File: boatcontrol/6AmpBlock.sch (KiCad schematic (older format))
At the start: 15 parts, among them U7901 ULN2803A

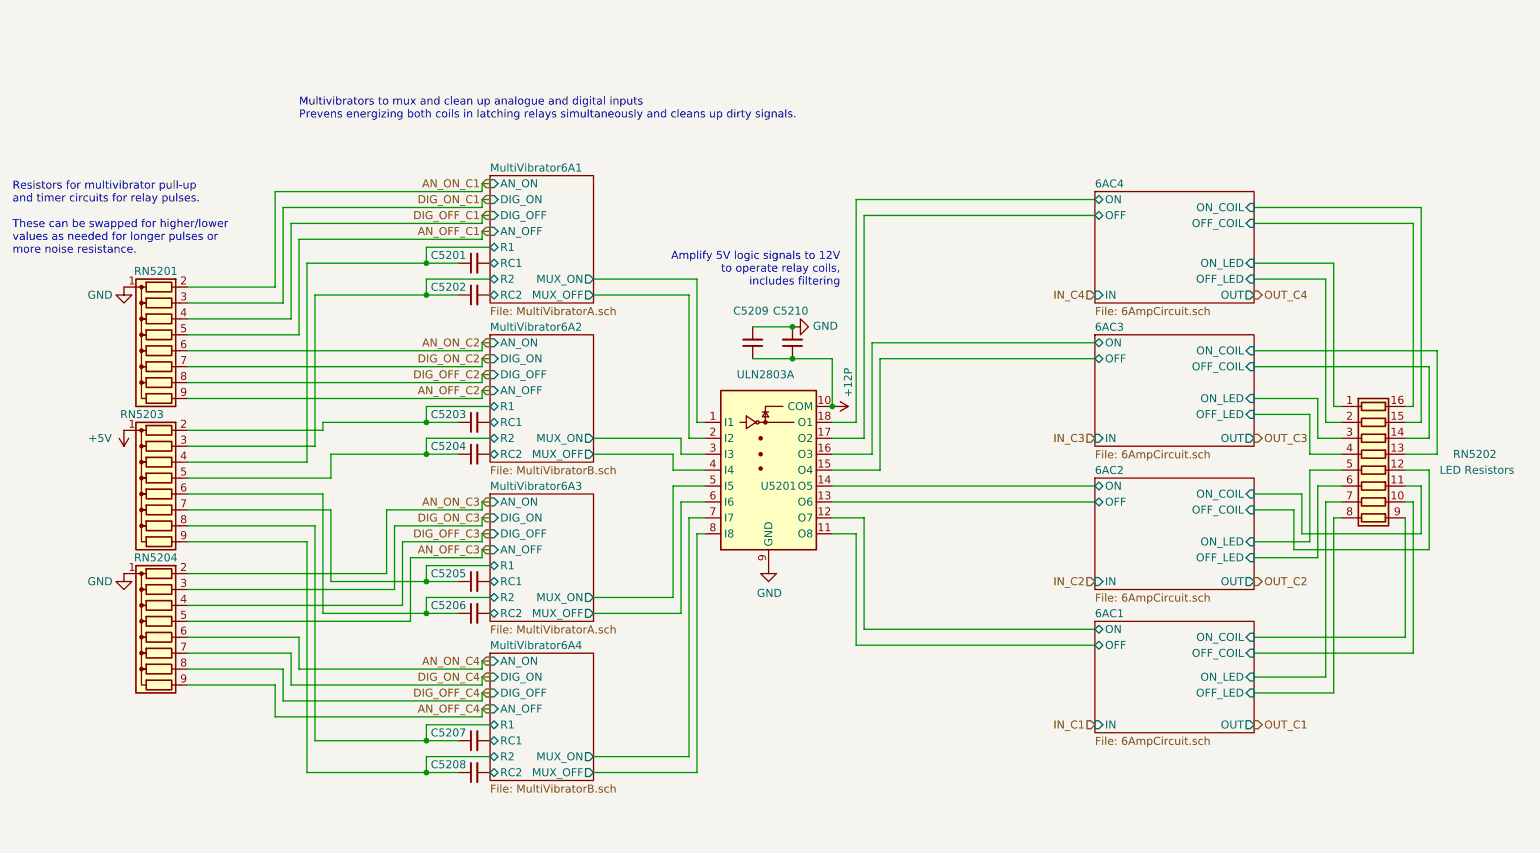
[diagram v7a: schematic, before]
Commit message: add second e-section
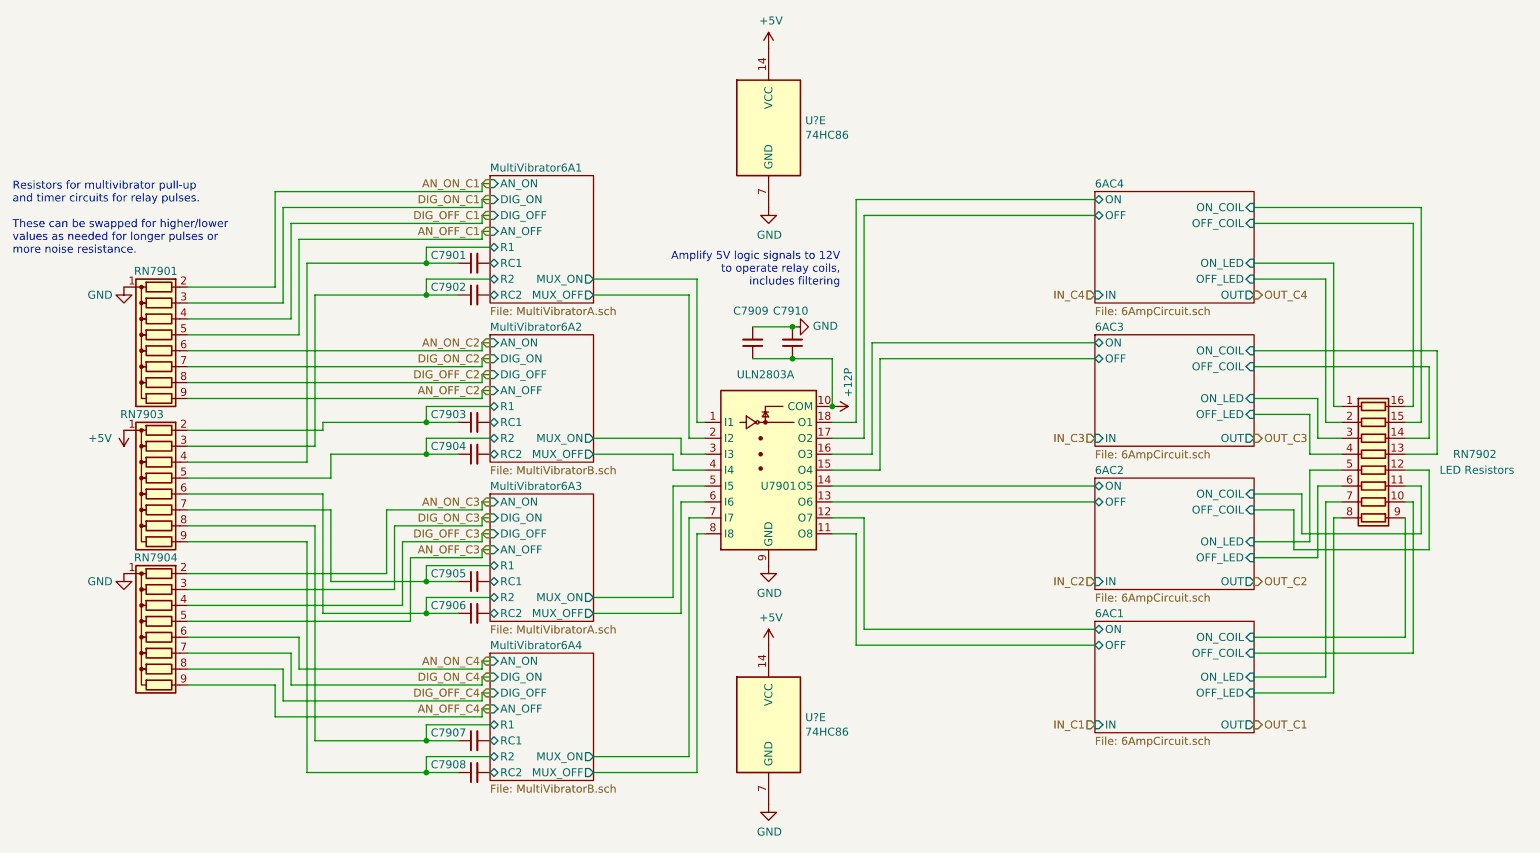
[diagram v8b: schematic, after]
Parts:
- added U? (x2): 74HC86, symbol 74xx:74HC86
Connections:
- net +5V: now also U?.14 (VCC), U?.14 (VCC)
- net GND: now also U?.7 (GND), U?.7 (GND)
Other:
- note removed: "Multivibrators to mux and clean up analogue and digital inputs\nPrevens energizing both coils in latching relays simultaneously and cleans up dirty signals."
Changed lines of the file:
@@
 $Descr A4 11693 8268
 encoding utf-8
-Sheet 40 97
+Sheet 67 97
 Title "Boat Control Hat"
 Date "2020-07-09"
@@
 AR Path="/D1BB8DB4/5F317CB5/60365AE4" Ref="#PWR07901"  Part="1"
 AR Path="/D1BB8DB4/5F746103/60365AE4" Ref="#PWR05201"  Part="1"
-F 0 "#PWR05201" H 6700 3400 50  0001 C CNN
+F 0 "#PWR07901" H 6700 3400 50  0001 C CNN
 F 1 "+12P" H 6550 3650 50  0000 C CNN
 F 2 "" H 6700 3550 50  0001 C CNN
@@
 AR Path="/D1BB8DB4/5F317CB5/60365AF1" Ref="U7901"  Part="1"
 AR Path="/D1BB8DB4/5F746103/60365AF1" Ref="U5201"  Part="1"
-F 0 "U5201" H 6250 3650 50  0000 L CNN
+F 0 "U7901" H 6250 3650 50  0000 L CNN
 F 1 "ULN2803A" H 6100 4350 50  0000 L CNN
 F 2 "Package_DIP:DIP-18_W7.62mm" H 6350 3200 50  0001 L CNN
@@
 Text HLabel 4550 4150 0    50   Output ~ 0
 AN_ON_C3
-Text Notes 3350 1750 0    50   ~ 0
-Multivibrators to mux and clean up analogue and digital inputs\nPrevens energizing both coils in latching relays simultaneously and cleans up dirty signals.
 Text Notes 6750 2800 2    50   ~ 0
 Amplify 5V logic signals to 12V\nto operate relay coils,\nincludes filtering
@@
 AR Path="/D1BB8DB4/5F317CB5/60365B03" Ref="#PWR07902"  Part="1"
 AR Path="/D1BB8DB4/5F746103/60365B03" Ref="#PWR05202"  Part="1"
-F 0 "#PWR05202" H 6300 4300 50  0001 C CNN
+F 0 "#PWR07902" H 6300 4300 50  0001 C CNN
 F 1 "GND" H 6305 4377 50  0000 C CNN
 F 2 "" H 6300 4550 50  0001 C CNN
@@
 AR Path="/D1BB8DB4/5F317CB5/60365C68" Ref="RN7902"  Part="1"
 AR Path="/D1BB8DB4/5F746103/60365C68" Ref="RN5202"  Part="1"
-F 0 "RN5202" V 10000 4450 50  0000 L CNN
+F 0 "RN7902" V 10000 4450 50  0000 L CNN
 F 1 "680Ω" V 9600 3800 50  0001 L CNN
 F 2 "BoatControl:DIP254P762X432-16P" V 10575 3950 50  0001 C CNN
@@
 AR Path="/D1BB8DB4/5F746103/62AB509B" Ref="C5201"  Part="1"
 AR Path="/D1BB8DB4/5F317CB5/62AB509B" Ref="C7901"  Part="1"
-F 0 "C5201" V 4400 2700 50  0000 L CNN
+F 0 "C7901" V 4400 2700 50  0000 L CNN
 F 1 "1µF" H 3600 2550 50  0001 L CNN
 F 2 "Capacitor_THT:C_Disc_D7.5mm_W5.0mm_P5.00mm" H 4450 2650 50  0001 C CNN
@@
 AR Path="/D1BB8DB4/5F746103/62AC1E93" Ref="C5202"  Part="1"
 AR Path="/D1BB8DB4/5F317CB5/62AC1E93" Ref="C7902"  Part="1"
-F 0 "C5202" V 4400 2900 50  0000 L CNN
+F 0 "C7902" V 4400 2900 50  0000 L CNN
 F 1 "1µF" H 3600 2750 50  0001 L CNN
 F 2 "Capacitor_THT:C_Disc_D7.5mm_W5.0mm_P5.00mm" H 4450 2850 50  0001 C CNN
@@
 AR Path="/D1BB8DB4/5F746103/62ADD9A6" Ref="C5208"  Part="1"
 AR Path="/D1BB8DB4/5F317CB5/62ADD9A6" Ref="C7908"  Part="1"
-F 0 "C5208" V 4400 5900 50  0000 L CNN
+F 0 "C7908" V 4400 5900 50  0000 L CNN
 F 1 "1µF" H 3600 5750 50  0001 L CNN
 F 2 "Capacitor_THT:C_Disc_D7.5mm_W5.0mm_P5.00mm" H 4450 5850 50  0001 C CNN
@@
 AR Path="/D1BB8DB4/5F746103/62AEACF8" Ref="C5207"  Part="1"
 AR Path="/D1BB8DB4/5F317CB5/62AEACF8" Ref="C7907"  Part="1"
-F 0 "C5207" V 4400 5700 50  0000 L CNN
+F 0 "C7907" V 4400 5700 50  0000 L CNN
 F 1 "1µF" H 3600 5550 50  0001 L CNN
 F 2 "Capacitor_THT:C_Disc_D7.5mm_W5.0mm_P5.00mm" H 4450 5650 50  0001 C CNN
@@
 AR Path="/D1BB8DB4/5F746103/62AF81A3" Ref="C5206"  Part="1"
 AR Path="/D1BB8DB4/5F317CB5/62AF81A3" Ref="C7906"  Part="1"
-F 0 "C5206" V 4400 4900 50  0000 L CNN
+F 0 "C7906" V 4400 4900 50  0000 L CNN
 F 1 "1µF" H 3600 4750 50  0001 L CNN
 F 2 "Capacitor_THT:C_Disc_D7.5mm_W5.0mm_P5.00mm" H 4450 4850 50  0001 C CNN
@@
 AR Path="/D1BB8DB4/5F746103/62B05762" Ref="C5205"  Part="1"
 AR Path="/D1BB8DB4/5F317CB5/62B05762" Ref="C7905"  Part="1"
-F 0 "C5205" V 4400 4700 50  0000 L CNN
+F 0 "C7905" V 4400 4700 50  0000 L CNN
 F 1 "1µF" H 3600 4550 50  0001 L CNN
 F 2 "Capacitor_THT:C_Disc_D7.5mm_W5.0mm_P5.00mm" H 4450 4650 50  0001 C CNN
@@
 AR Path="/D1BB8DB4/5F746103/62B3C5BA" Ref="C5203"  Part="1"
 AR Path="/D1BB8DB4/5F317CB5/62B3C5BA" Ref="C7903"  Part="1"
-F 0 "C5203" V 4400 3700 50  0000 L CNN
+F 0 "C7903" V 4400 3700 50  0000 L CNN
 F 1 "1µF" H 3600 3550 50  0001 L CNN
 F 2 "Capacitor_THT:C_Disc_D7.5mm_W5.0mm_P5.00mm" H 4450 3650 50  0001 C CNN
@@
 AR Path="/D1BB8DB4/5F746103/62B4996D" Ref="C5204"  Part="1"
 AR Path="/D1BB8DB4/5F317CB5/62B4996D" Ref="C7904"  Part="1"
-F 0 "C5204" V 4400 3900 50  0000 L CNN
+F 0 "C7904" V 4400 3900 50  0000 L CNN
 F 1 "1µF" H 3600 3750 50  0001 L CNN
 F 2 "Capacitor_THT:C_Disc_D7.5mm_W5.0mm_P5.00mm" H 4450 3850 50  0001 C CNN
@@
 AR Path="/D1BB8DB4/5F317CB5/62C7A7CE" Ref="RN7903"  Part="1"
 AR Path="/D1BB8DB4/5F746103/62C7A7CE" Ref="RN5203"  Part="1"
-F 0 "RN5203" V 1950 4050 50  0000 L CNN
+F 0 "RN7903" V 1950 4050 50  0000 L CNN
 F 1 "10MΩ" H 2100 3700 50  0001 L CNN
 F 2 "Resistor_THT:R_Array_SIP9" V 2925 4100 50  0001 C CNN
@@
 AR Path="/D1BB8DB4/5F317CB5/62F1D24C" Ref="RN7904"  Part="1"
 AR Path="/D1BB8DB4/5F746103/62F1D24C" Ref="RN5204"  Part="1"
-F 0 "RN5204" V 1950 5000 50  0000 C CNN
+F 0 "RN7904" V 1950 5000 50  0000 C CNN
 F 1 "100KΩ" V 2250 4700 50  0001 C CNN
 F 2 "Resistor_THT:R_Array_SIP9" H 3200 5100 50  0001 L CNN
@@
 AR Path="/D1BB8DB4/5F317CB5/62F2A731" Ref="RN7901"  Part="1"
 AR Path="/D1BB8DB4/5F746103/62F2A731" Ref="RN5201"  Part="1"
-F 0 "RN5201" V 1950 3200 50  0000 C CNN
+F 0 "RN7901" V 1950 3200 50  0000 C CNN
 F 1 "100KΩ" V 2250 2900 50  0001 C CNN
 F 2 "Resistor_THT:R_Array_SIP9" H 3200 3300 50  0001 L CNN
@@
 AR Path="/D1BB8DB4/5F317CB5/624D8B2F" Ref="C7909"  Part="1"
 AR Path="/D1BB8DB4/5F746103/624D8B2F" Ref="C5209"  Part="1"
-F 0 "C5209" H 6100 2950 50  0000 L CNN
+F 0 "C7909" H 6100 2950 50  0000 L CNN
 F 1 "10uF" H 6291 3105 50  0001 L CNN
 F 2 "Capacitor_THT:C_Disc_D7.5mm_W5.0mm_P5.00mm" H 6200 3150 50  0001 C CNN
@@
 AR Path="/D1BB8DB4/5F317CB5/624D8B37" Ref="C7910"  Part="1"
 AR Path="/D1BB8DB4/5F746103/624D8B37" Ref="C5210"  Part="1"
-F 0 "C5210" H 6350 2950 50  0000 L CNN
+F 0 "C7910" H 6350 2950 50  0000 L CNN
 F 1 "0.1uF" H 6541 3105 50  0001 L CNN
 F 2 "Capacitor_THT:C_Disc_D7.5mm_W5.0mm_P5.00mm" H 6450 3150 50  0001 C CNN
@@
 AR Path="/D1BB8DB4/5F317CB5/624D8B3E" Ref="#PWR0204"  Part="1"
 AR Path="/D1BB8DB4/5F746103/624D8B3E" Ref="#PWR0198"  Part="1"
-F 0 "#PWR0198" H 6450 2800 50  0001 C CNN
+F 0 "#PWR0204" H 6450 2800 50  0001 C CNN
 F 1 "GND" V 6455 2922 50  0000 R CNN
 F 2 "" H 6450 3050 50  0001 C CNN
@@
 	1    0    0    -1
 $EndComp
+$Comp
+L 74xx:74HC86 U?
+U 5 1 6036F096
+P 6300 5550
+AR Path="/D16552B4/5FA17F38/6036F096" Ref="U?"  Part="5"
+AR Path="/D16552B4/5FA17F52/6036F096" Ref="U?"  Part="5"
+AR Path="/D16552B4/5FA17F6C/6036F096" Ref="U?"  Part="5"
+AR Path="/D16552B4/5FA17F86/6036F096" Ref="U?"  Part="5"
+AR Path="/D1BB8DB4/5F317CB5/6036F096" Ref="U?"  Part="5"
+F 0 "U?" H 6530 5596 50  0000 L CNN
+F 1 "74HC86" H 6530 5505 50  0000 L CNN
+F 2 "" H 6300 5550 50  0001 C CNN
+F 3 "http://www.ti.com/lit/gpn/sn74HC86" H 6300 5550 50  0001 C CNN
+	5    6300 5550
+	1    0    0    -1
+$EndComp
+$Comp
+L power:+5V #PWR?
+U 1 1 6036F09C
+P 6300 5050
+AR Path="/D16552B4/5FA17F38/6036F09C" Ref="#PWR?"  Part="1"
+AR Path="/D16552B4/5FA17F52/6036F09C" Ref="#PWR?"  Part="1"
+AR Path="/D16552B4/5FA17F6C/6036F09C" Ref="#PWR?"  Part="1"
+AR Path="/D16552B4/5FA17F86/6036F09C" Ref="#PWR?"  Part="1"
+AR Path="/D1BB8DB4/5F317CB5/6036F09C" Ref="#PWR?"  Part="1"
+F 0 "#PWR?" H 6300 4900 50  0001 C CNN
+F 1 "+5V" H 6315 5223 50  0000 C CNN
+F 2 "" H 6300 5050 50  0001 C CNN
+F 3 "" H 6300 5050 50  0001 C CNN
+	1    6300 5050
+	1    0    0    -1
+$EndComp
+$Comp
+L power:GND #PWR?
+U 1 1 6036F0A2
+P 6300 6050
+AR Path="/D16552B4/5FA17F38/6036F0A2" Ref="#PWR?"  Part="1"
+AR Path="/D16552B4/5FA17F52/6036F0A2" Ref="#PWR?"  Part="1"
+AR Path="/D16552B4/5FA17F6C/6036F0A2" Ref="#PWR?"  Part="1"
+AR Path="/D16552B4/5FA17F86/6036F0A2" Ref="#PWR?"  Part="1"
+AR Path="/D1BB8DB4/5F317CB5/6036F0A2" Ref="#PWR?"  Part="1"
+F 0 "#PWR?" H 6300 5800 50  0001 C CNN
+F 1 "GND" H 6305 5877 50  0000 C CNN
+F 2 "" H 6300 6050 50  0001 C CNN
+F 3 "" H 6300 6050 50  0001 C CNN
+	1    6300 6050
+	1    0    0    -1
+$EndComp
+$Comp
+L 74xx:74HC86 U?
+U 5 1 60382869
+P 6300 1800
+AR Path="/D16552B4/5FA17F38/60382869" Ref="U?"  Part="5"
+AR Path="/D16552B4/5FA17F52/60382869" Ref="U?"  Part="5"
+AR Path="/D16552B4/5FA17F6C/60382869" Ref="U?"  Part="5"
+AR Path="/D16552B4/5FA17F86/60382869" Ref="U?"  Part="5"
+AR Path="/D1BB8DB4/5F317CB5/60382869" Ref="U?"  Part="5"
+F 0 "U?" H 6530 1846 50  0000 L CNN
+F 1 "74HC86" H 6530 1755 50  0000 L CNN
+F 2 "" H 6300 1800 50  0001 C CNN
+F 3 "http://www.ti.com/lit/gpn/sn74HC86" H 6300 1800 50  0001 C CNN
+	5    6300 1800
+	1    0    0    -1
+$EndComp
+$Comp
+L power:+5V #PWR?
+U 1 1 6038286F
+P 6300 1300
+AR Path="/D16552B4/5FA17F38/6038286F" Ref="#PWR?"  Part="1"
+AR Path="/D16552B4/5FA17F52/6038286F" Ref="#PWR?"  Part="1"
+AR Path="/D16552B4/5FA17F6C/6038286F" Ref="#PWR?"  Part="1"
+AR Path="/D16552B4/5FA17F86/6038286F" Ref="#PWR?"  Part="1"
+AR Path="/D1BB8DB4/5F317CB5/6038286F" Ref="#PWR?"  Part="1"
+F 0 "#PWR?" H 6300 1150 50  0001 C CNN
+F 1 "+5V" H 6315 1473 50  0000 C CNN
+F 2 "" H 6300 1300 50  0001 C CNN
+F 3 "" H 6300 1300 50  0001 C CNN
+	1    6300 1300
+	1    0    0    -1
+$EndComp
+$Comp
+L power:GND #PWR?
+U 1 1 60382875
+P 6300 2300
+AR Path="/D16552B4/5FA17F38/60382875" Ref="#PWR?"  Part="1"
+AR Path="/D16552B4/5FA17F52/60382875" Ref="#PWR?"  Part="1"
+AR Path="/D16552B4/5FA17F6C/60382875" Ref="#PWR?"  Part="1"
+AR Path="/D16552B4/5FA17F86/60382875" Ref="#PWR?"  Part="1"
+AR Path="/D1BB8DB4/5F317CB5/60382875" Ref="#PWR?"  Part="1"
+F 0 "#PWR?" H 6300 2050 50  0001 C CNN
+F 1 "GND" H 6305 2127 50  0000 C CNN
+F 2 "" H 6300 2300 50  0001 C CNN
+F 3 "" H 6300 2300 50  0001 C CNN
+	1    6300 2300
+	1    0    0    -1
+$EndComp
